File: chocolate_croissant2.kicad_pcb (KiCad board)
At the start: 2 copper layers, 85 x 56 mm, 4 parts, among them U1 Pico

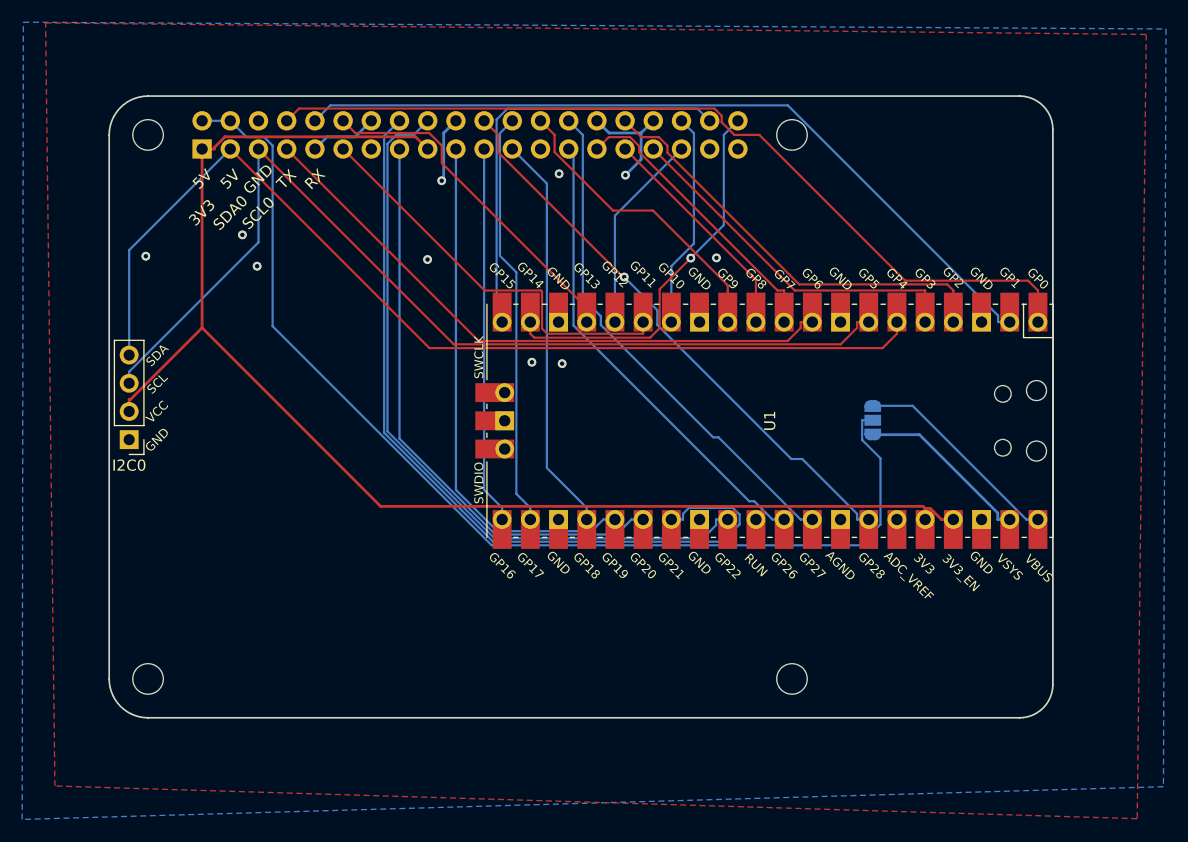
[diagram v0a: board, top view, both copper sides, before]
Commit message: Image of the back of the PCB added to README.
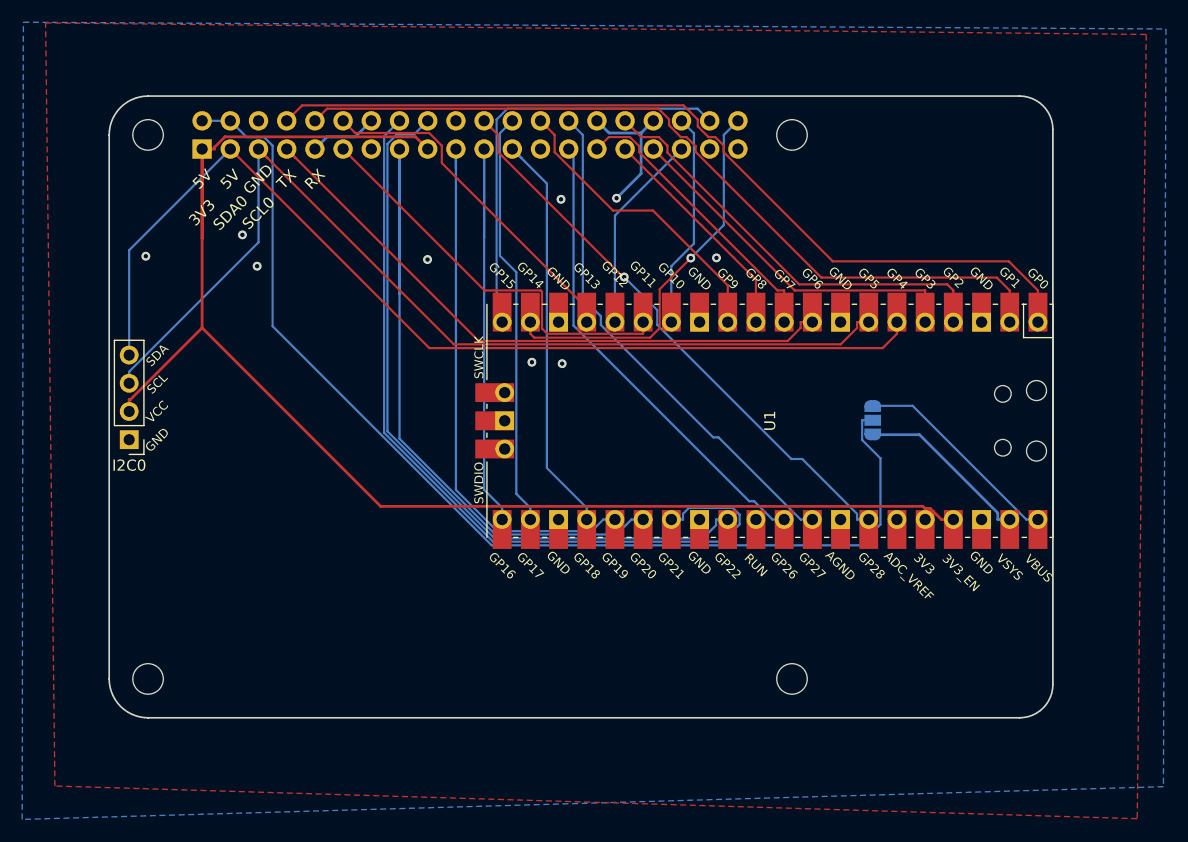
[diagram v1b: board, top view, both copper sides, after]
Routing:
- net GPIO20: track 52.2 -> 65.2 mm
- net +3V3: track 123.5 -> 131.6 mm
- net SPI0_MISO: track 34.0 -> 42.0 mm
- net GND: track 22.4 -> 18.9 mm, vias 10 -> 9
- net SPI0_MOSI: track 47.0 -> 48.8 mm
- net RX: track 71.6 -> 73.3 mm
- net I2C0_SCL: track 89.3 -> 90.5 mm
- net SPI0_SCK: track 36.1 -> 37.3 mm
- net GPIO6: track 55.5 -> 56.7 mm
- net I2C1_SCL: track 45.9 -> 46.8 mm
- net GPIO9: track 27.2 -> 28.1 mm
- net GPIO23: track 51.5 -> 52.4 mm
- net GPIO10: track 19.4 -> 20.2 mm
- net SPI1_MOSI: track 38.5 -> 39.3 mm
- net GPIO7: track 26.2 -> 27.0 mm
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
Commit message: SPI breakouts and new images.
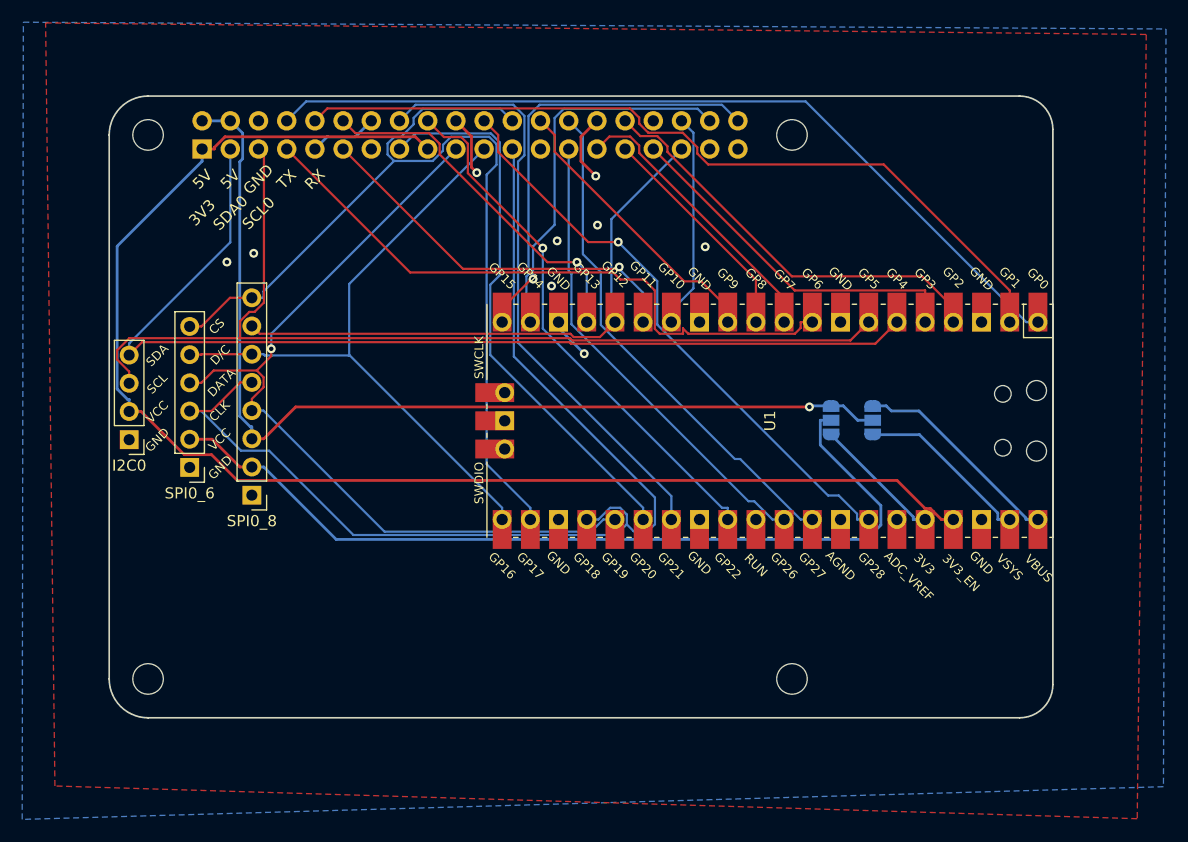
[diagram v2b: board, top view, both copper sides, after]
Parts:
- removed JP1: SolderJumper_3_Open, Jumper:SolderJumper-3_P1.3mm_Open_RoundedPad1.0x1.5mm_NumberLabels
- added PI_5V_SEL1: SolderJumper_3_Open, Jumper:SolderJumper-3_P1.3mm_Open_RoundedPad1.0x1.5mm_NumberLabels, B.Cu at (177.6, 88.9)
- added SPI0_6: Conn_01x06, Connector_PinHeader_2.54mm:PinHeader_1x06_P2.54mm_Vertical, F.Cu at (116.1, 93.2)
- added SPI0_8: Conn_01x08, Connector_PinHeader_2.54mm:PinHeader_1x08_P2.54mm_Vertical, F.Cu at (121.7, 95.7)
- added SPI_VCC_SEL1: SolderJumper_3_Open, Jumper:SolderJumper-3_P1.3mm_Open_RoundedPad1.0x1.5mm_NumberLabels, B.Cu at (173.8, 88.9)
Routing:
- net SPI_VCC: track 0.00 -> 79.2 mm
- net SPI0_SCK: track 37.3 -> 98.4 mm
- net SPI0_CS: track 37.5 -> 86.6 mm
- net SPI1_MISO: track 18.1 -> 52.0 mm
- net SPI0_MOSI: track 48.8 -> 75.9 mm, vias 0 -> 1
- net GPIO21: track 73.4 -> 54.6 mm
- net GPIO22: track 66.0 -> 48.3 mm, vias 0 -> 1
- net SPI0_MISO: track 42.0 -> 58.6 mm
- net GPIO20: track 65.2 -> 50.0 mm
- net +5V: track 98.3 -> 90.0 mm, vias 0 -> 1
- net +3V3: track 131.6 -> 139.7 mm
- net SPI1_MOSI: track 39.3 -> 35.2 mm, vias 0 -> 1
- net SPI1_SCK: track 34.8 -> 38.7 mm, vias 1 -> 0
- net GND: track 18.9 -> 21.5 mm
- net GPIO9: track 28.1 -> 26.0 mm
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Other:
- board text added: "CLK"
- board text added: "CS"
- board text added: "D/C"
- board text added: "DATA"

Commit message: Adding some more stuff, more documentation in the README etc.
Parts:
- added DEBUG1: QWIIC_CONNECTORJS-1MM, Connector_JST:JST_SH_SM04B-SRSS-TB_1x04-1MP_P1.00mm_Horizontal, F.Cu at (140.7, 112.7)
- added I2C0QT1: QWIIC_CONNECTORJS-1MM, Connector_JST:JST_SH_SM04B-SRSS-TB_1x04-1MP_P1.00mm_Horizontal, F.Cu at (111.8, 75.5)
- moved U1 27.6 mm to (142.8, 78.5)
- moved SPI0_8 2.17 mm to (121.7, 97.8)
- moved SPI0_6 2.15 mm to (116.1, 95.3)
- moved I2C0 2.10 mm to (110.6, 92.8)
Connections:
- SPI0_8 pad 2: SPI_VCC -> +3V3
- U1 pad 41: unconnected-(U1-Pad41) -> DEBUG_CLK
- U1 pad 43: unconnected-(U1-Pad43) -> DEBUG_DATA
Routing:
- net DEBUG_CLK: track 0.00 -> 59.4 mm
- net DEBUG_DATA: track 0.00 -> 52.0 mm
- net +3V3: track 139.7 -> 167.3 mm, vias 0 -> 1
- net +5V: track 90.0 -> 113.7 mm
- net SPI0_CS: track 86.6 -> 66.3 mm, vias 0 -> 1
- net GPIO8: track 20.5 -> 35.8 mm
- net I2C0_SDA: track 92.8 -> 108.2 mm
- net GND: track 21.5 -> 35.5 mm
- net GPIO23: track 53.0 -> 66.5 mm, vias 1 -> 0
- net SPI0_MISO: track 58.6 -> 71.7 mm, vias 0 -> 1
- net GPIO10: track 19.4 -> 29.5 mm
- net SPI0_SCK: track 98.4 -> 90.5 mm
- net SPI0_MOSI: track 75.9 -> 82.1 mm, vias 1 -> 0
- net SPI1_SCK: track 38.7 -> 33.9 mm, vias 0 -> 1
- net I2C0_SCL: track 90.8 -> 95.1 mm, vias 0 -> 1
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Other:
- board text added: "+3.3V"
- board text added: "RST"
- board text added: "VIN"

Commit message: KiCad 7 plus local footprints and symbols.
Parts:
- RP1: footprint Raspberry-Pi-4-library-for-kicad:raspberrypi_2_3 -> chocolate_croissant:raspberrypi_2_3
- U1: footprint RPi_Pico:RPi_Pico_SMD_TH -> chocolate_croissant:RPi_Pico_SMD_TH
